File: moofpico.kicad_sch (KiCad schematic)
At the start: 22 parts, among them J1 Conn_01x04, J100 Bus_Apple_II_Card_Side, J2 Micro_SD_Card_Det2, Q1 BS170, SW1 SW_DIP_x02, U2 74F11, U3 74LVC245, U4 74LVC245, U5 74LVC245, U6 RaspberryPi_Pico

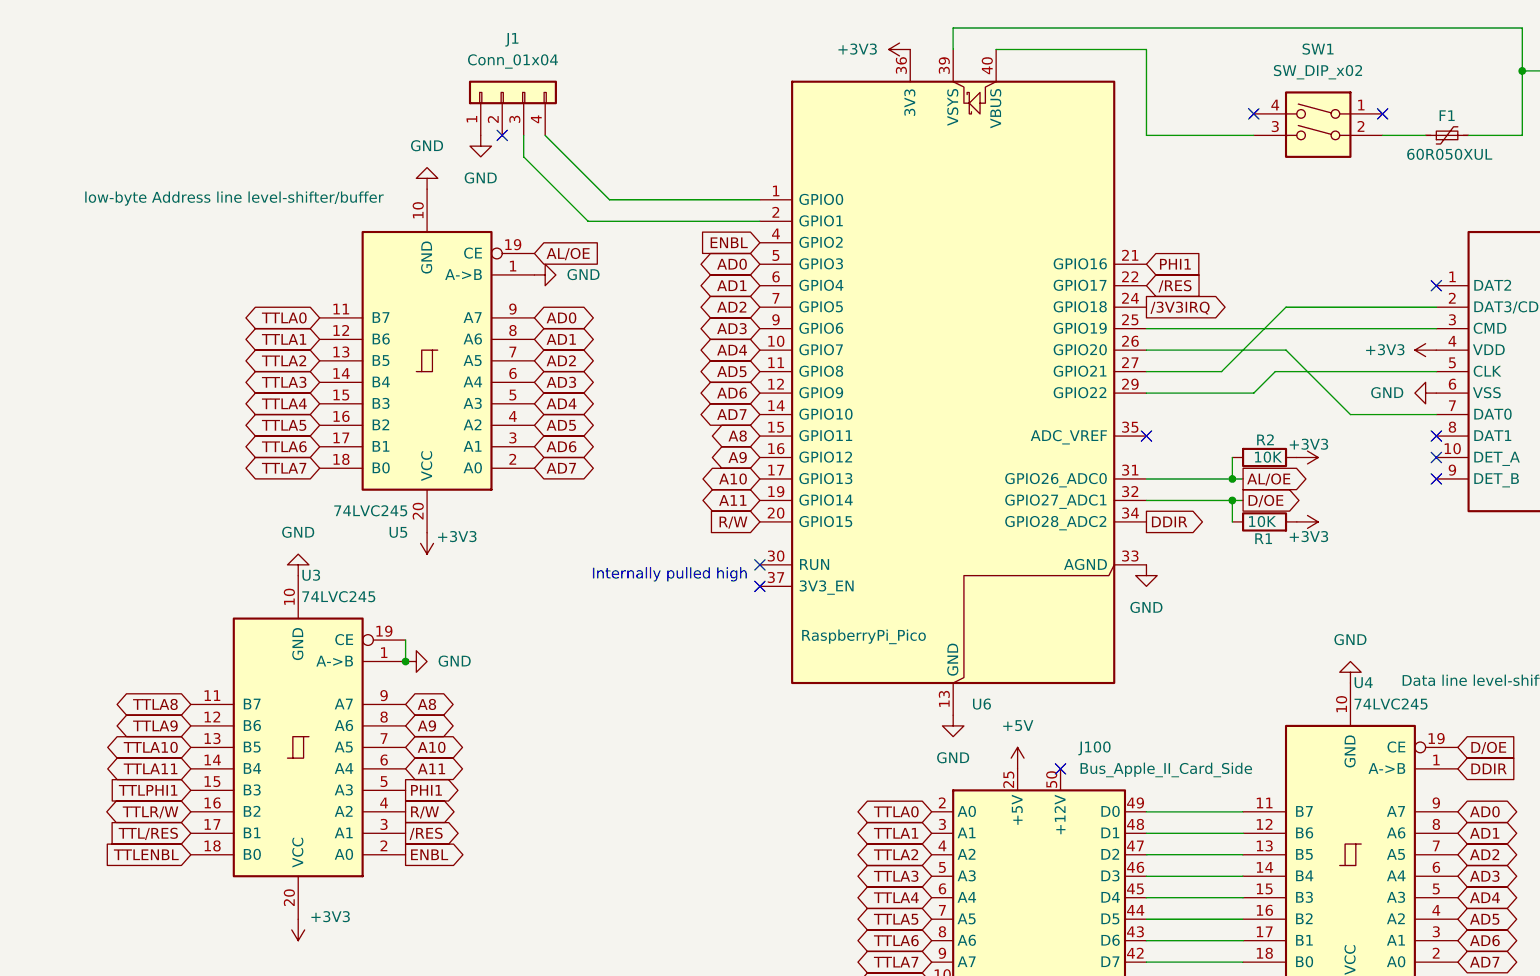
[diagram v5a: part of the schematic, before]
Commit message: move to 1x dip (even though it's more expensive than 2x?); swap enbl and phi1 to make the pcb layout ever so slightly nicer
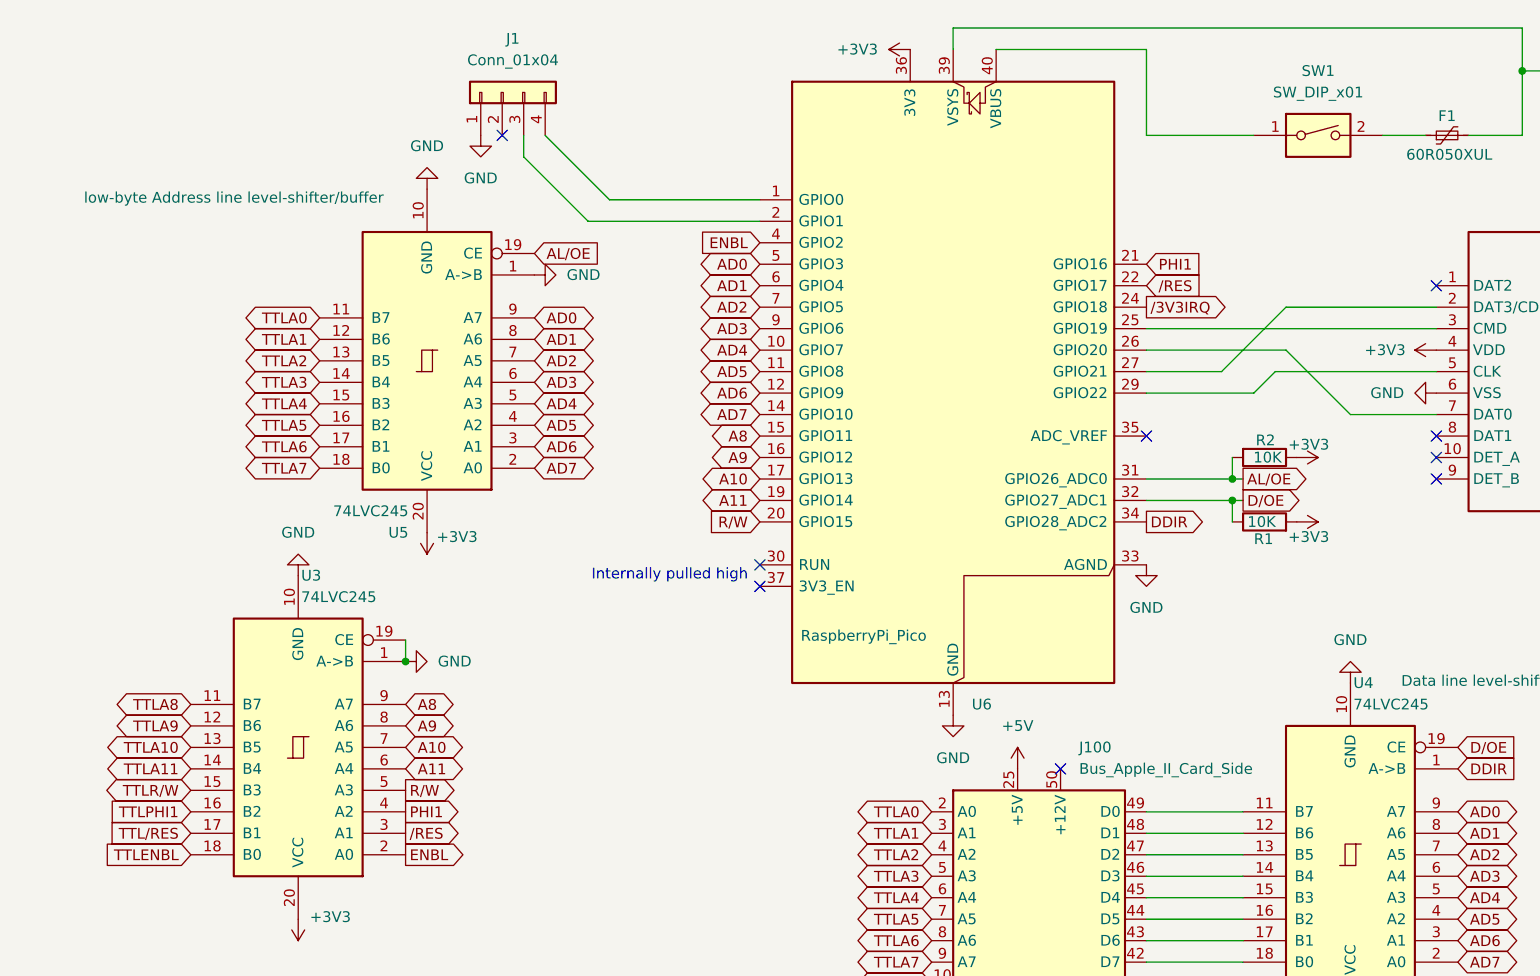
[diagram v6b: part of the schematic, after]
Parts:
- removed SW1: SW_DIP_x02, Button_Switch_THT:SW_DIP_SPSTx02_Slide_9.78x7.26mm_W7.62mm_P2.54mm, symbol Switch:SW_DIP_x02
- added SW1: SW_DIP_x01, Button_Switch_THT:SW_DIP_SPSTx01_Slide_6.7x4.1mm_W7.62mm_P2.54mm_LowProfile, symbol Switch:SW_DIP_x01
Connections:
- net PHI1: now also U3.4 (A2); no longer U3.5 (A3)
- net R/W: now also U3.5 (A3); no longer U3.4 (A2)
- net TTLPHI1: now also U3.16 (B2); no longer U3.15 (B3)
- net TTLR/W: now also U3.15 (B3); no longer U3.16 (B2)
- net at F1.1: now also SW1.2
- net at U6.40 (VBUS): now also SW1.1
- no-connect marks 28 -> 26
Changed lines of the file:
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@@
 	)
 	(no_connect
-		(at 172.72 26.67)
-	)
-	(no_connect
 		(at 119.38 182.88)
 	)
@@
 	)
 	(no_connect
-		(at 157.48 26.67)
-	)
-	(no_connect
 		(at 144.78 180.34)
 	)
@@
 	(global_label "PHI1"
 		(shape output)
-		(at 57.15 106.68 0)
+		(at 57.15 109.22 0)
 		(fields_autoplaced yes)
 		(effects
@@
 		)
 		(property "Intersheetrefs" "${INTERSHEET_REFS}"
-			(at 64.55 106.68 0)
+			(at 64.55 109.22 0)
 			(effects
 				(font
@@
 	(global_label "TTLPHI1"
 		(shape input)
-		(at 31.75 106.68 180)
+		(at 31.75 109.22 180)
 		(fields_autoplaced yes)
 		(effects
@@
 		)
 		(property "Intersheetrefs" "${INTERSHEET_REFS}"
-			(at 21.3867 106.68 0)
+			(at 21.3867 109.22 0)
 			(effects
 				(font
@@
 	(global_label "TTLR{slash}W"
 		(shape tri_state)
-		(at 31.75 109.22 180)
+		(at 31.75 106.68 180)
 		(fields_autoplaced yes)
 		(effects
@@
 		)
 		(property "Intersheetrefs" "${INTERSHEET_REFS}"
-			(at 21.7496 109.22 0)
+			(at 21.7496 106.68 0)
 			(effects
 				(font
@@
 	(global_label "R{slash}W"
 		(shape output)
-		(at 57.15 109.22 0)
+		(at 57.15 106.68 0)
 		(fields_autoplaced yes)
 		(effects
@@
 		)
 		(property "Intersheetrefs" "${INTERSHEET_REFS}"
-			(at 64.1871 109.22 0)
+			(at 64.1871 106.68 0)
 			(effects
 				(font
@@
 	)
 	(symbol
-		(lib_id "Switch:SW_DIP_x02")
-		(at 165.1 29.21 0)
-		(mirror y)
-		(unit 1)
-		(exclude_from_sim no)
-		(in_bom yes)
-		(on_board yes)
-		(dnp no)
-		(property "Reference" "SW1"
-			(at 165.1 19.05 0)
-			(effects
-				(font
-					(size 1.27 1.27)
-				)
-			)
-		)
-		(property "Value" "SW_DIP_x02"
-			(at 165.1 21.59 0)
-			(effects
-				(font
-					(size 1.27 1.27)
-				)
-			)
-		)
-		(property "Footprint" "Button_Switch_THT:SW_DIP_SPSTx02_Slide_9.78x7.26mm_W7.62mm_P2.54mm"
-			(at 165.1 29.21 0)
-			(effects
-				(font
-					(size 1.27 1.27)
-				)
-				(hide yes)
-			)
-		)
-		(property "Datasheet" "https://www.mouser.com/datasheet/2/418/7/ENG_CD_1825360_B5-2021008.pdf"
-			(at 165.1 29.21 0)
-			(effects
-				(font
-					(size 1.27 1.27)
-				)
-				(hide yes)
-			)
-		)
-		(property "Description" "2x DIP Switch, Single Pole Single Throw (SPST) switch, small symbol"
-			(at 165.1 29.21 0)
-			(effects
-				(font
-					(size 1.27 1.27)
-				)
-				(hide yes)
-			)
-		)
-		(pin "2"
-		)
-		(pin "1"
-		)
-		(pin "4"
-		)
-		(pin "3"
-		)
-		(instances
-			(project "moofpico"
-				(path "/adf04048-7c47-4d7c-943c-c55ccf696419"
-					(reference "SW1")
-					(unit 1)
-				)
-			)
-		)
-	)
-	(symbol
 		(lib_id "Device:C_Small")
 		(at 41.91 139.7 0)
@@
 					(unit 1)
 				)
+			)
+		)
+	)
+	(symbol
+		(lib_id "Switch:SW_DIP_x01")
+		(at 165.1 29.21 0)
+		(unit 1)
+		(exclude_from_sim no)
+		(in_bom yes)
+		(on_board yes)
+		(dnp no)
+		(fields_autoplaced yes)
+		(property "Reference" "SW1"
+			(at 165.1 21.59 0)
+			(effects
+				(font
+					(size 1.27 1.27)
+				)
+			)
+		)
+		(property "Value" "SW_DIP_x01"
+			(at 165.1 24.13 0)
+			(effects
+				(font
+					(size 1.27 1.27)
+				)
+			)
+		)
+		(property "Footprint" "Button_Switch_THT:SW_DIP_SPSTx01_Slide_6.7x4.1mm_W7.62mm_P2.54mm_LowProfile"
+			(at 165.1 29.21 0)
+			(effects
+				(font
+					(size 1.27 1.27)
+				)
+				(hide yes)
+			)
+		)
+		(property "Datasheet" "~"
+			(at 165.1 29.21 0)
+			(effects
+				(font
+					(size 1.27 1.27)
+				)
+				(hide yes)
+			)
+		)
+		(property "Description" "1x DIP Switch, Single Pole Single Throw (SPST) switch, small symbol"
+			(at 165.1 29.21 0)
+			(effects
+				(font
+					(size 1.27 1.27)
+				)
+				(hide yes)
+			)
+		)
+		(pin "2"
+		)
+		(pin "1"
+		)
+		(instances
+			(project "moofpico"
+				(path "/adf04048-7c47-4d7c-943c-c55ccf696419"
+					(reference "SW1")
+					(unit 1)
+				)

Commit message: minor fiddling, NFCI
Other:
- note added: "Enable USB power for Pico (when Apple II PSU is off)"
- moved on the sheet: C2, ZD1
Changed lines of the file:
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@@
 	)
 	(junction
-		(at 189.23 21.59)
+		(at 222.25 72.39)
 		(diameter 0)
 		(color 0 0 0 0)
 	)
 	(junction
-		(at 222.25 72.39)
+		(at 93.98 172.72)
 		(diameter 0)
 		(color 0 0 0 0)
 	)
 	(junction
-		(at 93.98 172.72)
+		(at 158.75 16.51)
 		(diameter 0)
 		(color 0 0 0 0)
@@
 	)
 	(junction
-		(at 209.55 99.06)
+		(at 151.13 16.51)
 		(diameter 0)
 		(color 0 0 0 0)
 	)
 	(junction
-		(at 199.39 21.59)
+		(at 209.55 99.06)
 		(diameter 0)
 		(color 0 0 0 0)
 	)
 	(junction
-		(at 154.94 69.85)
+		(at 189.23 29.21)
 		(diameter 0)
 		(color 0 0 0 0)
@@
 	)
 	(junction
-		(at 41.91 142.24)
+		(at 154.94 69.85)
 		(diameter 0)
 		(color 0 0 0 0)
 	)
 	(junction
-		(at 57.15 91.44)
+		(at 41.91 142.24)
 		(diameter 0)
 		(color 0 0 0 0)
 	)
 	(junction
-		(at 194.31 21.59)
+		(at 57.15 91.44)
 		(diameter 0)
 		(color 0 0 0 0)
@@
 	(wire
 		(pts
+			(xy 189.23 16.51) (xy 189.23 29.21)
+		)
+		(stroke
+			(width 0)
+			(type default)
+		)
+	)
+	(wire
+		(pts
 			(xy 154.94 72.39) (xy 156.21 72.39)
 		)
@@
 	(wire
 		(pts
+			(xy 210.82 29.21) (xy 210.82 21.59)
+		)
+		(stroke
+			(width 0)
+			(type default)
+		)
+	)
+	(wire
+		(pts
 			(xy 144.78 54.61) (xy 161.29 54.61)
 		)
@@
 	(wire
 		(pts
-			(xy 189.23 21.59) (xy 194.31 21.59)
+			(xy 189.23 29.21) (xy 198.12 29.21)
 		)
 		(stroke
@@
 	(wire
 		(pts
-			(xy 121.92 16.51) (xy 189.23 16.51)
+			(xy 121.92 16.51) (xy 151.13 16.51)
 		)
 		(stroke
@@
 	(wire
 		(pts
-			(xy 194.31 21.59) (xy 199.39 21.59)
-		)
-		(stroke
-			(width 0)
-			(type default)
-		)
-	)
-	(wire
-		(pts
 			(xy 33.02 142.24) (xy 41.91 142.24)
 		)
@@
 	(wire
 		(pts
-			(xy 154.94 67.31) (xy 154.94 69.85)
+			(xy 210.82 21.59) (xy 217.17 21.59)
 		)
 		(stroke
@@
 	(wire
 		(pts
-			(xy 99.06 36.83) (xy 81.28 36.83)
+			(xy 154.94 67.31) (xy 154.94 69.85)
 		)
 		(stroke
@@
 	(wire
 		(pts
-			(xy 199.39 21.59) (xy 203.2 21.59)
+			(xy 99.06 36.83) (xy 81.28 36.83)
 		)
 		(stroke
@@
 	(wire
 		(pts
-			(xy 189.23 21.59) (xy 189.23 29.21)
-		)
-		(stroke
-			(width 0)
-			(type default)
-		)
-	)
-	(wire
-		(pts
 			(xy 41.91 135.89) (xy 41.91 137.16)
 		)
@@
 	(wire
 		(pts
-			(xy 210.82 21.59) (xy 217.17 21.59)
+			(xy 205.74 29.21) (xy 210.82 29.21)
 		)
 		(stroke
@@
 	(wire
 		(pts
+			(xy 151.13 16.51) (xy 158.75 16.51)
+		)
+		(stroke
+			(width 0)
+			(type default)
+		)
+	)
+	(wire
+		(pts
 			(xy 144.78 59.69) (xy 157.48 59.69)
 		)
@@
 	(wire
 		(pts
-			(xy 161.29 49.53) (xy 179.07 49.53)
+			(xy 158.75 16.51) (xy 189.23 16.51)
 		)
 		(stroke
@@
 	(wire
 		(pts
-			(xy 168.91 62.23) (xy 179.07 62.23)
+			(xy 161.29 49.53) (xy 179.07 49.53)
 		)
 		(stroke
@@
 	(wire
 		(pts
-			(xy 144.78 52.07) (xy 179.07 52.07)
+			(xy 168.91 62.23) (xy 179.07 62.23)
 		)
 		(stroke
@@
 	(wire
 		(pts
-			(xy 144.78 127) (xy 156.21 127)
+			(xy 144.78 52.07) (xy 179.07 52.07)
 		)
 		(stroke
@@
 	(wire
 		(pts
-			(xy 189.23 16.51) (xy 189.23 21.59)
+			(xy 144.78 127) (xy 156.21 127)
 		)
 		(stroke
@@
 		)
 	)
+	(text "Enable USB power for Pico\n(when Apple II PSU is off)"
+		(exclude_from_sim no)
+		(at 165.608 34.544 0)
+		(effects
+			(font
+				(size 1.27 1.27)
+			)
+		)
+	)
 	(text "Internally pulled high"
 		(exclude_from_sim no)
@@
 	(symbol
 		(lib_id "power:PWR_FLAG")
-		(at 199.39 21.59 0)
+		(at 158.75 16.51 180)
 		(unit 1)
 		(exclude_from_sim no)
@@
 		(fields_autoplaced yes)
 		(property "Reference" "#FLG01"
-			(at 199.39 19.685 0)
+			(at 158.75 18.415 0)
 			(effects
 				(font
@@
 		)
 		(property "Value" "PWR_FLAG"
-			(at 199.39 16.51 0)
+			(at 161.29 17.7799 0)
 			(effects
 				(font
 					(size 1.27 1.27)
 				)
+				(justify right)
 			)
 		)
 		(property "Footprint" ""
-			(at 199.39 21.59 0)
+			(at 158.75 16.51 0)
 			(effects
 				(font
@@
 		)
 		(property "Datasheet" "~"
-			(at 199.39 21.59 0)
+			(at 158.75 16.51 0)
 			(effects
 				(font
@@
 		)
 		(property "Description" "Special symbol for telling ERC where power comes from"
-			(at 199.39 21.59 0)
+			(at 158.75 16.51 0)
 			(effects
 				(font
@@
 	(symbol
 		(lib_id "Device:C_Small")
-		(at 194.31 24.13 0)
+		(at 151.13 19.05 0)
 		(unit 1)
 		(exclude_from_sim no)
@@
 		(dnp no)
 		(property "Reference" "C2"
-			(at 196.342 24.384 0)
+			(at 153.162 19.304 0)
 			(effects
 				(font
@@
 		)
 		(property "Value" ".1u"
-			(at 195.834 26.416 0)
+			(at 152.654 21.336 0)
 			(effects
 				(font
@@
 		)
 		(property "Footprint" "Capacitor_THT:C_Disc_D3.8mm_W2.6mm_P2.50mm"
-			(at 194.31 24.13 0)
+			(at 151.13 19.05 0)
 			(effects
 				(font
@@
 		)
 		(property "Datasheet" "https://www.vishay.com/docs/45171/kseries.pdf"
-			(at 194.31 24.13 0)
+			(at 151.13 19.05 0)
 			(effects
 				(font
@@
 		)
 		(property "Description" "Unpolarized capacitor, small symbol"
-			(at 194.31 24.13 0)
+			(at 151.13 19.05 0)
 			(effects
 				(font
@@
 	(symbol
 		(lib_id "Diode:1N5819")
-		(at 207.01 21.59 0)
+		(at 201.93 29.21 0)
 		(unit 1)
 		(exclude_from_sim no)
@@
 		(dnp no)
 		(property "Reference" "ZD1"
-			(at 207.01 19.05 0)
+			(at 201.93 26.67 0)
 			(effects
 				(font
@@
 		)
 		(property "Value" "1N5819"
-			(at 207.01 24.384 0)
+			(at 201.93 32.004 0)
 			(effects
 				(font
@@
 		)
 		(property "Footprint" "Diode_THT:D_DO-41_SOD81_P7.62mm_Horizontal"
-			(at 207.01 26.035 0)
+			(at 201.93 33.655 0)
 			(effects
 				(font
@@
 		)
 		(property "Datasheet" "http://www.vishay.com/docs/88525/1n5817.pdf"
-			(at 207.01 21.59 0)
+			(at 201.93 29.21 0)
 			(effects
 				(font
@@
 		)
 		(property "Description" "40V 1A Schottky Barrier Rectifier Diode, DO-41"
-			(at 207.01 21.59 0)
+			(at 201.93 29.21 0)
 			(effects
 				(font
@@
 	(symbol
 		(lib_id "power:GND")
-		(at 194.31 26.67 0)
+		(at 151.13 21.59 0)
 		(unit 1)
 		(exclude_from_sim no)
@@
 		(fields_autoplaced yes)
 		(property "Reference" "#PWR05"
-			(at 194.31 33.02 0)
+			(at 151.13 27.94 0)
 			(effects
 				(font
@@
 		)
 		(property "Value" "GND"
-			(at 194.31 31.75 0)
+			(at 151.13 26.67 0)
 			(effects
 				(font
@@
 		)
 		(property "Footprint" ""
-			(at 194.31 26.67 0)
+			(at 151.13 21.59 0)
 			(effects
 				(font
@@
 		)
 		(property "Datasheet" ""
-			(at 194.31 26.67 0)
+			(at 151.13 21.59 0)
 			(effects
 				(font
@@
 		)
 		(property "Description" "Power symbol creates a global label with name \"GND\" , ground"
-			(at 194.31 26.67 0)
+			(at 151.13 21.59 0)
 			(effects
 				(font
@@
 		(on_board yes)
 		(dnp no)
-		(fields_autoplaced yes)
 		(property "Reference" "SW1"
-			(at 165.1 21.59 0)
+			(at 165.1 25.4 0)
 			(effects
 				(font
@@
 					(size 1.27 1.27)
 				)
+				(hide yes)
 			)
 		)
@@
 			)
 		)
-		(property "Description" "1x DIP Switch, Single Pole Single Throw (SPST) switch, small symbol"
-			(at 165.1 29.21 0)
+		(property "Description" "Enable USB power for pico when the II is turned off"
+			(at 167.132 33.528 0)
 			(effects
 				(font
